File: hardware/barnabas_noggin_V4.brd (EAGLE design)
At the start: 100 x 80 mm, 60 parts, among them J1 POWER_JACKPTH, J10 2.54mm, J2 ICSP, J3 ICSP, J4 USB-mini-90 -SMD, J5 ICSP, J6 2.54mm, J7 2.54mm, J8 2.54mm, J9 2.54mm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

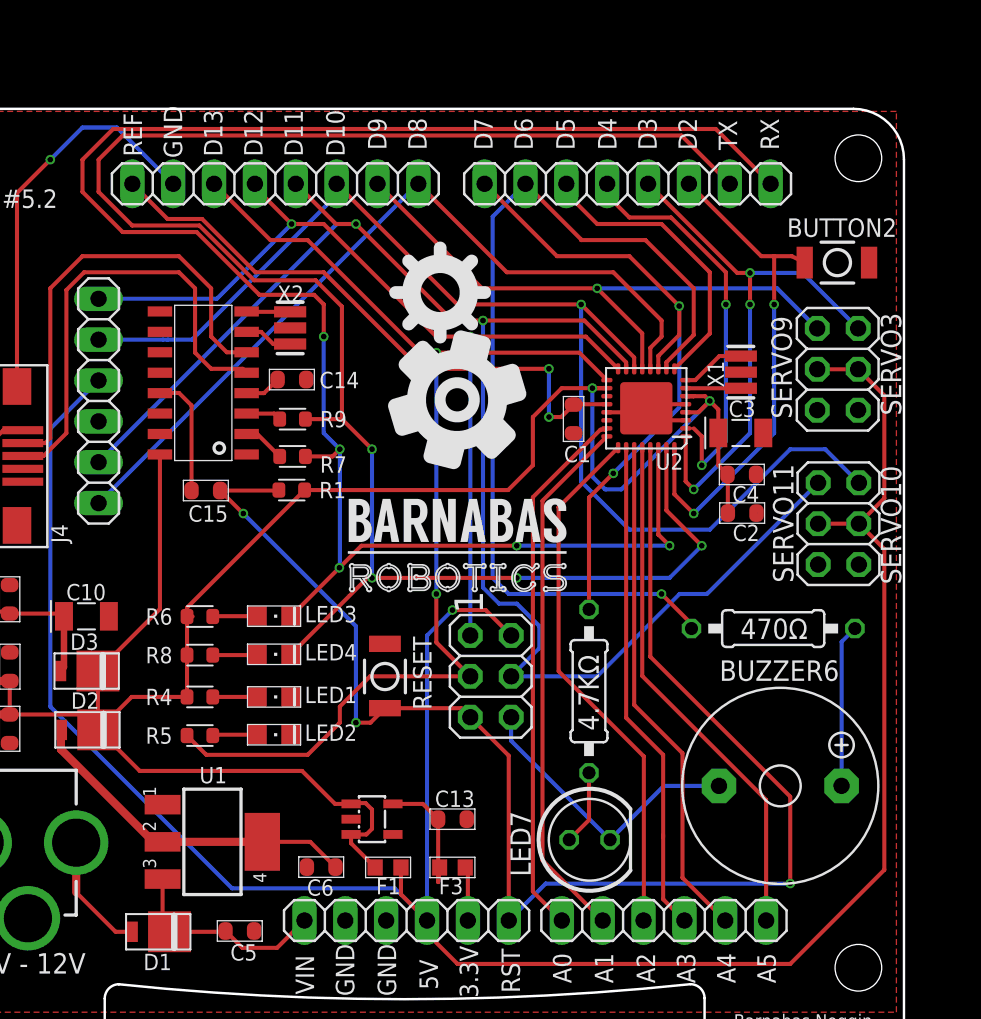
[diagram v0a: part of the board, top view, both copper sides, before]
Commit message: Replaced with new ATMEGA328 chip and modified PWM pins
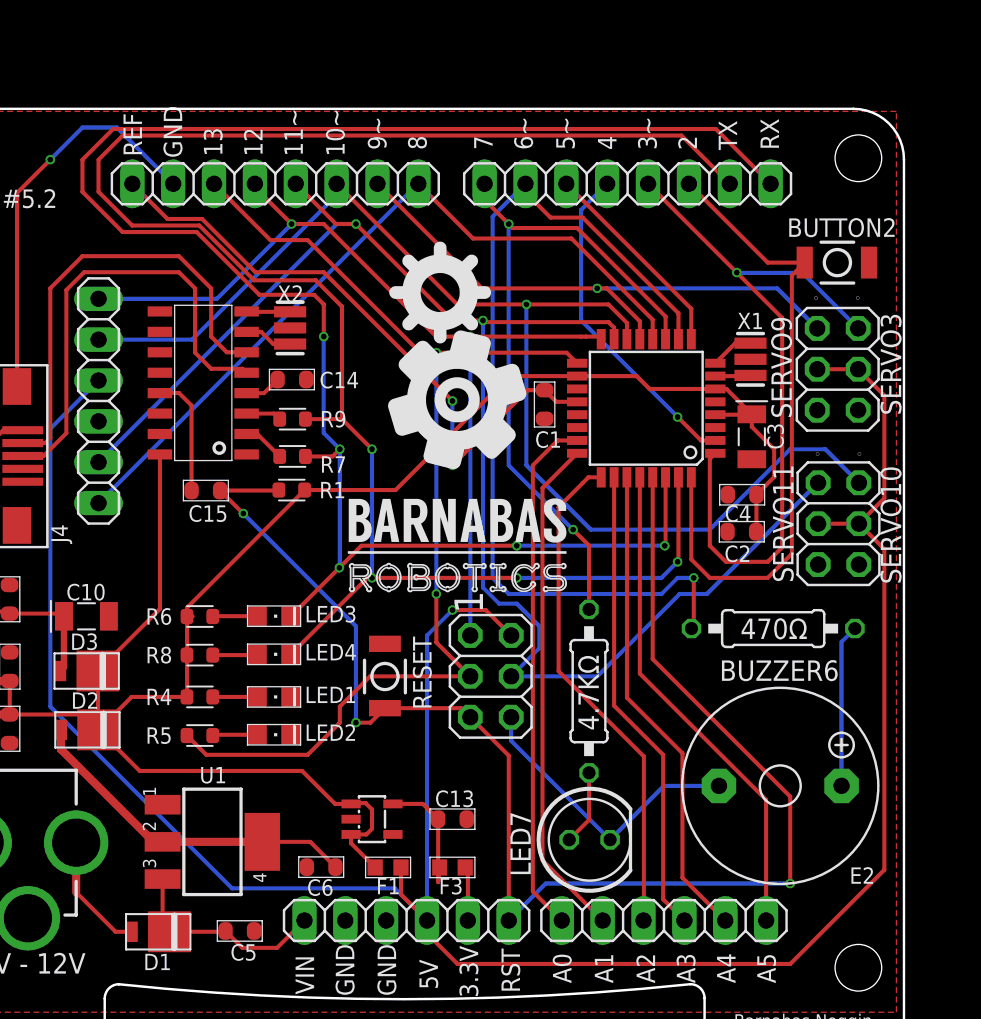
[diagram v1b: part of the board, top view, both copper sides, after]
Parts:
- U2: value ATMEGA328P-32MUR -> ATMEGA328P-AU; device barnabas_noggin_V4:VQFN32 -> barnabas_noggin_V4:TQFP32-08
- moved C3 2.38 mm to (60.6, 43.2), turned to 270 degrees
- moved C1 2.01 mm to (47.7, 43.8)
- moved C4 1.26 mm to (60.0, 38.2), turned to 180 degrees
- moved C2 1.16 mm to (60.0, 35.9), turned to 180 degrees
- moved X1 1.00 mm to (60.5, 46.6)
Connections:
- net GND: no longer U2.33
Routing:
- net D3: track 35.2 -> 46.2 mm, vias 3 -> 1
- net 5V: track 131.3 -> 122.8 mm, vias 2 -> 0
- net D2: track 31.8 -> 40.1 mm, vias 2 -> 0
- net GND: track 51.1 -> 43.2 mm
- net D5: track 18.5 -> 12.9 mm
- net D4: track 25.7 -> 20.6 mm, vias 2 -> 1
- net TX: track 116.4 -> 112.8 mm
- net D8: track 50.1 -> 47.4 mm
- net RX: track 115.7 -> 113.3 mm
- net D13/SCK: track 71.2 -> 68.9 mm
- net D12/MISO: track 60.2 -> 58.2 mm
- net RESET: track 92.1 -> 90.2 mm
- net D7: track 40.9 -> 42.7 mm
- net A1: track 33.3 -> 31.5 mm
- net A2: track 33.1 -> 31.3 mm
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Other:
- board text added: "10~"
- board text added: "11~"
- board text added: "12"
- board text added: "13"
- board text added: "2"
- board text added: "3~"
- board text added: "4"
- board text added: "5~"
- board text added: "6~"
- board text added: "7"
- board text added: "8"
- board text added: "9~"
- board text removed: "D10"
- board text removed: "D11"
- board text removed: "D12"
- board text removed: "D13"
- board text removed: "D2"
- board text removed: "D3"
- board text removed: "D4"
- board text removed: "D5"
- board text removed: "D6"
- board text removed: "D7"
- board text removed: "D8"
- board text removed: "D9"

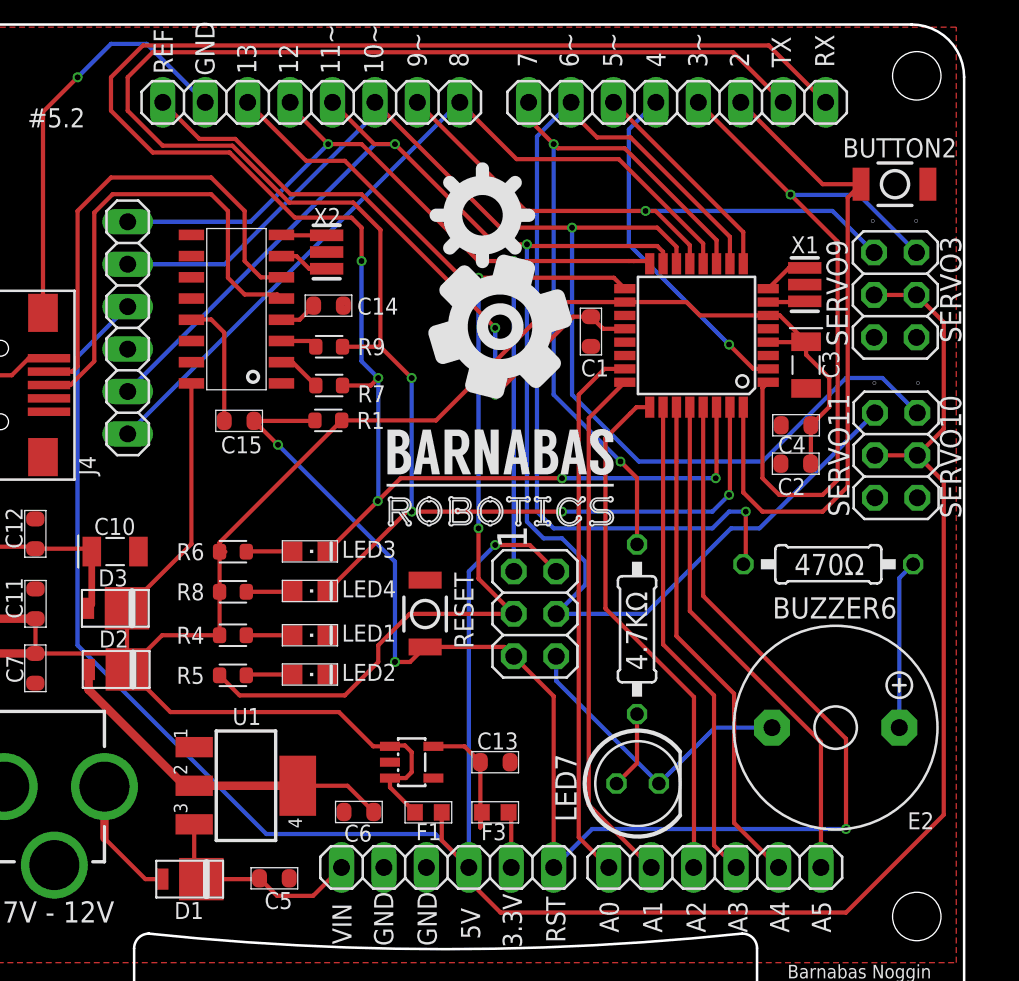
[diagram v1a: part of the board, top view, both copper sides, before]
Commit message: Replaced fuses. Added pull-up resistor for pin 2.
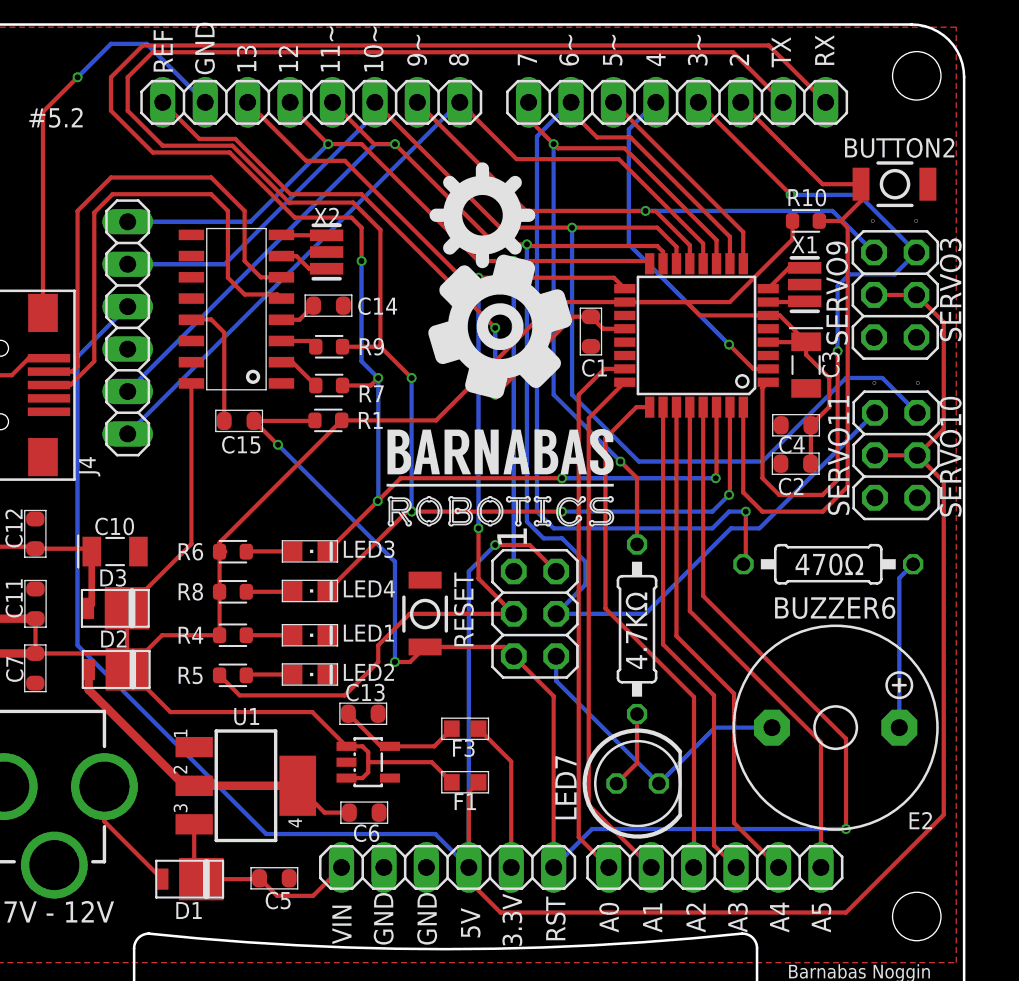
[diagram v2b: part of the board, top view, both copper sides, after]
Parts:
- added R10: 1K, barnabas_noggin_V4:R0603
- moved C13 8.42 mm to (34.1, 20.9)
- moved F3 5.31 mm to (40.2, 20.0)
- moved F1 2.84 mm to (40.2, 16.8)
- moved U3 2.60 mm to (34.4, 18.0)
- moved C6 0.32 mm to (34.2, 15.0), turned to 0 degrees
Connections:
- net 5V: now also R10.2
- net D2: now also R10.1
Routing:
- net 5V: track 122.8 -> 135.7 mm
- net 3.3V_PIN: track 3.37 -> 9.11 mm
- net D2: track 40.1 -> 41.7 mm
- net VOUT: track 21.3 -> 19.9 mm
- net 5V_PIN: track 149.3 -> 150.7 mm
- net D3: track 46.2 -> 45.1 mm, vias 1 -> 2
- net 3.3V: track 8.03 -> 7.43 mm
- net N$16: track 7.55 -> 6.97 mm
